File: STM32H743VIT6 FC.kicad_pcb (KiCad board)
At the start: 2 copper layers, 37 x 37 mm, 6 parts, among them J4 Conn_01x04_Male

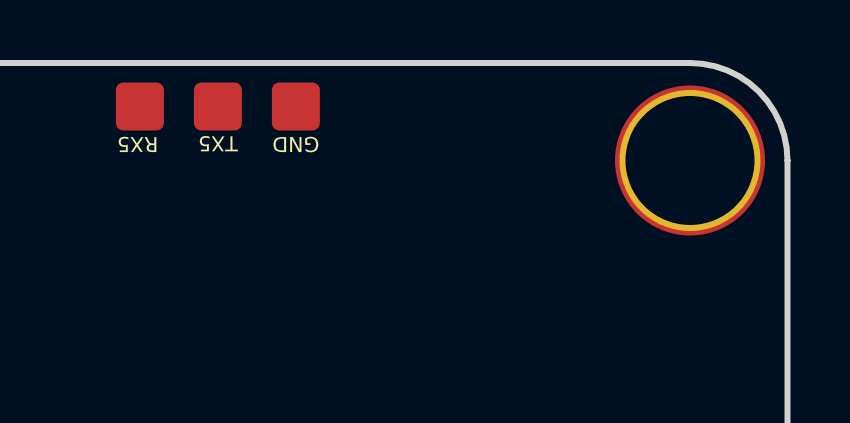
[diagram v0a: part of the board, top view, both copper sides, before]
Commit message: Added footprints.
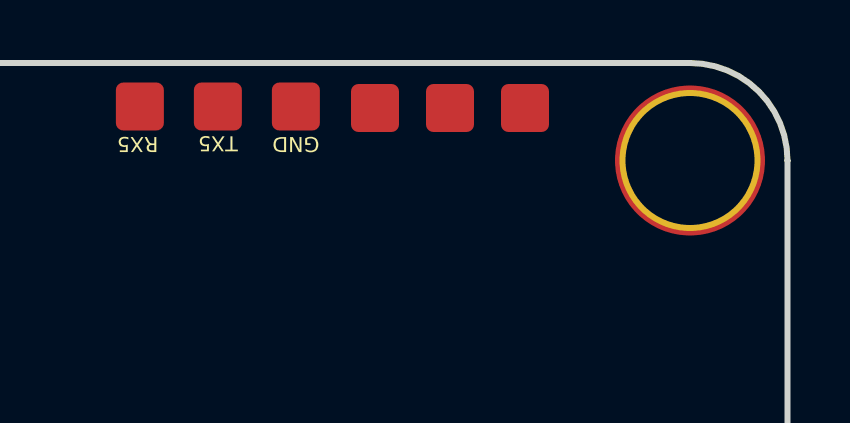
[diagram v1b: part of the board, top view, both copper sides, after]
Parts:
- added REF**: Pads_1x3, All:Pads_1x3, F.Cu at (173.0, 103.2)
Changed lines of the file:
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@@
+		(embedded_fonts no)
+	)
+	(footprint "All:Pads_1x3"
+		(layer "F.Cu")
+		(at 173 103.25)
+		(property "Reference" "REF**"
+			(at -0.3 1.1 0)
+			(unlocked yes)
+			(layer "F.SilkS")
+			(hide yes)
+			(effects
+				(font
+					(size 1 1)
+					(thickness 0.1)
+				)
+			)
+		)
+		(property "Value" "Pads_1x3"
+			(at 0 1 0)
+			(unlocked yes)
+			(layer "F.Fab")
+			(hide yes)
+			(effects
+				(font
+					(size 1 1)
+					(thickness 0.15)
+				)
+			)
+		)
+		(property "Datasheet" ""
+			(at 0 0 0)
+			(unlocked yes)
+			(layer "F.Fab")
+			(hide yes)
+			(effects
+				(font
+					(size 1 1)
+					(thickness 0.15)
+				)
+			)
+		)
+		(property "Description" ""
+			(at 0 0 0)
+			(unlocked yes)
+			(layer "F.Fab")
+			(hide yes)
+			(effects
+				(font
+					(size 1 1)
+					(thickness 0.15)
+				)
+			)
+		)
+		(attr smd)
+		(fp_line
+			(start -1.25 -1.25)
+			(end -1.25 1.25)
+			(stroke
+				(width 0.05)
+				(type solid)
+			)
+			(layer "F.CrtYd")
+		)
+		(fp_line
+			(start 1.25 -1.25)
+			(end 1.25 1.25)
+			(stroke
+				(width 0.05)
+				(type solid)
+			)
+			(layer "F.CrtYd")
+		)
+		(fp_rect
+			(start -3.75 -1.25)
+			(end 3.75 1.25)
+			(stroke
+				(width 0.05)
+				(type solid)
+			)
+			(fill no)
+			(layer "F.CrtYd")
+		)
+		(pad "1" smd roundrect
+			(at -2.5 0 180)
+			(size 1.6 1.6)
+			(layers "F.Cu" "F.Mask" "F.Paste")
+			(roundrect_rratio 0.15625)
+		)
+		(pad "2" smd roundrect
+			(at 0 0 180)
+			(size 1.6 1.6)
+			(layers "F.Cu" "F.Mask" "F.Paste")
+			(roundrect_rratio 0.15625)
+		)
+		(pad "3" smd roundrect
+			(at 2.5 0 180)
+			(size 1.6 1.6)
+			(layers "F.Cu" "F.Mask" "F.Paste")
+			(roundrect_rratio 0.15625)
+		)
 		(embedded_fonts no)
 	)

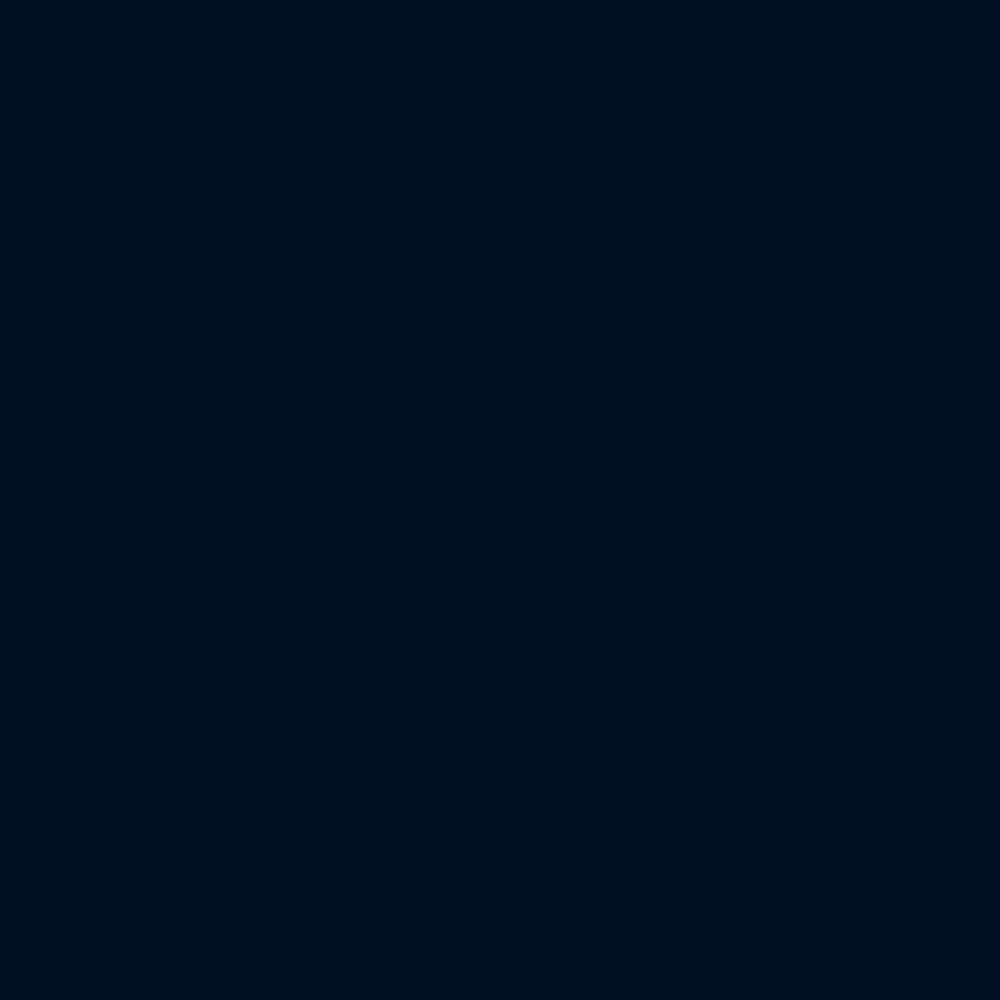
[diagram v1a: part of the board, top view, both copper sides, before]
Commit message: Added 3D models.
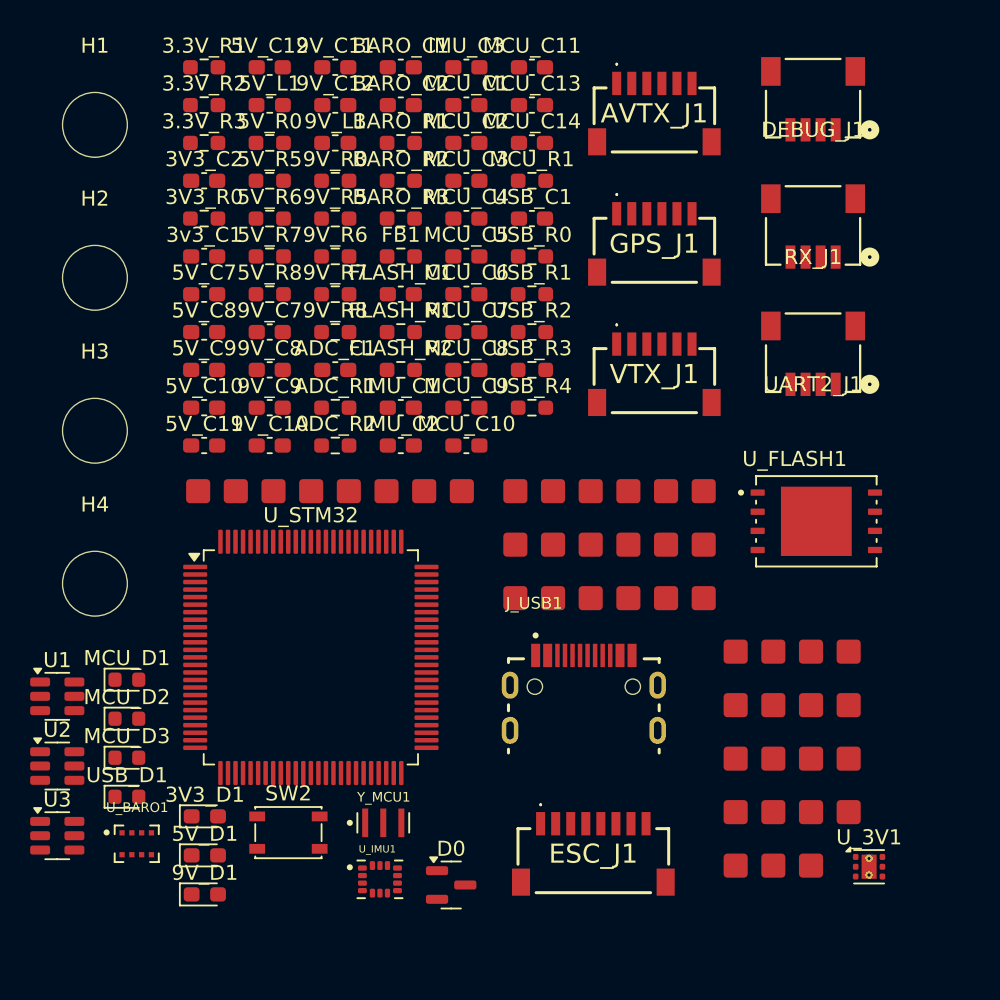
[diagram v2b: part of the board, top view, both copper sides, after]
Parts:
- added 3.3V_R1: 150, Resistor_SMD:R_0603_1608Metric_Pad0.98x0.95mm_HandSolder, F.Cu at (84.2, 36.8)
- added 3.3V_R2: 150, Resistor_SMD:R_0603_1608Metric_Pad0.98x0.95mm_HandSolder, F.Cu at (84.2, 39.3)
- added 3.3V_R3: 150, Resistor_SMD:R_0603_1608Metric_Pad0.98x0.95mm_HandSolder, F.Cu at (84.2, 41.8)
- added 3V3_C2: 1u, Capacitor_SMD:C_0603_1608Metric_Pad1.08x0.95mm_HandSolder, F.Cu at (84.2, 44.3)
- added 3V3_D1: RED, LED_SMD:LED_0603_1608Metric_Pad1.05x0.95mm_HandSolder, F.Cu at (84.3, 86.5)
- added 3V3_R0: 150, Resistor_SMD:R_0603_1608Metric_Pad0.98x0.95mm_HandSolder, F.Cu at (84.2, 46.8)
- added 3v3_C1: 1u, Capacitor_SMD:C_0603_1608Metric_Pad1.08x0.95mm_HandSolder, F.Cu at (84.2, 49.3)
- added 5V_C10: 22u, Capacitor_SMD:C_0603_1608Metric_Pad1.08x0.95mm_HandSolder, F.Cu at (84.2, 59.4)
- added 5V_C11: 22u, Capacitor_SMD:C_0603_1608Metric_Pad1.08x0.95mm_HandSolder, F.Cu at (84.2, 61.9)
- added 5V_C12: 75p, Capacitor_SMD:C_0603_1608Metric_Pad1.08x0.95mm_HandSolder, F.Cu at (88.6, 36.8)
- added 5V_C7: 10u, Capacitor_SMD:C_0603_1608Metric_Pad1.08x0.95mm_HandSolder, F.Cu at (84.2, 51.9)
- added 5V_C8: 100n, Capacitor_SMD:C_0603_1608Metric_Pad1.08x0.95mm_HandSolder, F.Cu at (84.2, 54.4)
- added 5V_C9: 100n, Capacitor_SMD:C_0603_1608Metric_Pad1.08x0.95mm_HandSolder, F.Cu at (84.2, 56.9)
- added 5V_D1: RED, LED_SMD:LED_0603_1608Metric_Pad1.05x0.95mm_HandSolder, F.Cu at (84.3, 89.1)
- added 5V_L1: 10u, Inductor_SMD:L_0603_1608Metric_Pad1.05x0.95mm_HandSolder, F.Cu at (88.6, 39.3)
- added 5V_R0: 330, Resistor_SMD:R_0603_1608Metric_Pad0.98x0.95mm_HandSolder, F.Cu at (88.6, 41.8)
- added 5V_R5: 511k, Resistor_SMD:R_0603_1608Metric_Pad0.98x0.95mm_HandSolder, F.Cu at (88.6, 44.3)
- added 5V_R6: 105k, Resistor_SMD:R_0603_1608Metric_Pad0.98x0.95mm_HandSolder, F.Cu at (88.6, 46.8)
- added 5V_R7: 100k, Resistor_SMD:R_0603_1608Metric_Pad0.98x0.95mm_HandSolder, F.Cu at (88.6, 49.3)
- added 5V_R8: 13k, Resistor_SMD:R_0603_1608Metric_Pad0.98x0.95mm_HandSolder, F.Cu at (88.6, 51.9)
- added 9V_C10: 22u, Capacitor_SMD:C_0603_1608Metric_Pad1.08x0.95mm_HandSolder, F.Cu at (88.6, 61.9)
- added 9V_C11: 22u, Capacitor_SMD:C_0603_1608Metric_Pad1.08x0.95mm_HandSolder, F.Cu at (92.9, 36.8)
- added 9V_C12: 75p, Capacitor_SMD:C_0603_1608Metric_Pad1.08x0.95mm_HandSolder, F.Cu at (92.9, 39.3)
- added 9V_C7: 10u, Capacitor_SMD:C_0603_1608Metric_Pad1.08x0.95mm_HandSolder, F.Cu at (88.6, 54.4)
- added 9V_C8: 100n, Capacitor_SMD:C_0603_1608Metric_Pad1.08x0.95mm_HandSolder, F.Cu at (88.6, 56.9)
- added 9V_C9: 100n, Capacitor_SMD:C_0603_1608Metric_Pad1.08x0.95mm_HandSolder, F.Cu at (88.6, 59.4)
- added 9V_D1: RED, LED_SMD:LED_0603_1608Metric_Pad1.05x0.95mm_HandSolder, F.Cu at (84.3, 91.7)
- added 9V_L1: 15u, Inductor_SMD:L_0603_1608Metric_Pad1.05x0.95mm_HandSolder, F.Cu at (92.9, 41.8)
- added 9V_R0: 750, Resistor_SMD:R_0603_1608Metric_Pad0.98x0.95mm_HandSolder, F.Cu at (92.9, 44.3)
- added 9V_R5: 511k, Resistor_SMD:R_0603_1608Metric_Pad0.98x0.95mm_HandSolder, F.Cu at (92.9, 46.8)
- added 9V_R6: 105k, Resistor_SMD:R_0603_1608Metric_Pad0.98x0.95mm_HandSolder, F.Cu at (92.9, 49.3)
- added 9V_R7: 100k, Resistor_SMD:R_0603_1608Metric_Pad0.98x0.95mm_HandSolder, F.Cu at (92.9, 51.9)
- added 9V_R8: 7k, Resistor_SMD:R_0603_1608Metric_Pad0.98x0.95mm_HandSolder, F.Cu at (92.9, 54.4)
- added ADC_C1: 100n, Capacitor_SMD:C_0603_1608Metric_Pad1.08x0.95mm_HandSolder, F.Cu at (92.9, 56.9)
- added ADC_R1: 15k, Resistor_SMD:R_0603_1608Metric_Pad0.98x0.95mm_HandSolder, F.Cu at (92.9, 59.4)
- added ADC_R2: 15k, Resistor_SMD:R_0603_1608Metric_Pad0.98x0.95mm_HandSolder, F.Cu at (92.9, 61.9)
- added AVTX_J1: SM06B-SRSS-TB, All:SM06BSRSSTBLFSN, F.Cu at (114.1, 40.1)
- added AVTX_J2: pads, All:Pads_1x6, F.Cu at (111.1, 64.9)
- added BARO_C1: 100n, Capacitor_SMD:C_0603_1608Metric_Pad1.08x0.95mm_HandSolder, F.Cu at (97.3, 36.8)
- added BARO_C2: 100n, Capacitor_SMD:C_0603_1608Metric_Pad1.08x0.95mm_HandSolder, F.Cu at (97.3, 39.3)
- added BARO_R1: 10k, Resistor_SMD:R_0603_1608Metric_Pad0.98x0.95mm_HandSolder, F.Cu at (97.3, 41.8)
- added BARO_R2: 10k, Resistor_SMD:R_0603_1608Metric_Pad0.98x0.95mm_HandSolder, F.Cu at (97.3, 44.3)
- added BARO_R3: 10k, Resistor_SMD:R_0603_1608Metric_Pad0.98x0.95mm_HandSolder, F.Cu at (97.3, 46.8)
- added CAM_J2: pads, All:Pads_1x3, F.Cu at (122.0, 89.8)
- added D0: BAT54C, Package_TO_SOT_SMD:SOT-23, F.Cu at (100.6, 91.1)
- added DEBUG_J1: SM04B-SRSS-TB, All:CONN_SM04B-SRSS-TB_JST, F.Cu at (124.6, 38.8)
- added DEBUG_J2: pads, All:Pads_1x4, F.Cu at (123.3, 75.6)
- added ESC_J1: SM08B-SRSS-TB, All:SM08BSRSSTB, F.Cu at (110.1, 89.3)
- added ESC_J2: pads, All:Pads_1x8, F.Cu at (92.6, 64.9)
- added FB1: FCM 1608KF-102T02, Resistor_SMD:R_0603_1608Metric_Pad0.98x0.95mm_HandSolder, F.Cu at (97.3, 49.3)
- added FLASH_C1: 100n, Capacitor_SMD:C_0603_1608Metric_Pad1.08x0.95mm_HandSolder, F.Cu at (97.3, 51.9)
- added FLASH_R1: 10k, Resistor_SMD:R_0603_1608Metric_Pad0.98x0.95mm_HandSolder, F.Cu at (97.3, 54.4)
- added FLASH_R2: 10k, Resistor_SMD:R_0603_1608Metric_Pad0.98x0.95mm_HandSolder, F.Cu at (97.3, 56.9)
- added GPS_J1: SM06B-SRSS-TB, All:SM06BSRSSTBLFSN, F.Cu at (114.1, 48.8)
- added GPS_J2: pads, All:Pads_1x6, F.Cu at (111.1, 68.5)
- added H1: MountingHole, MountingHole:MountingHole_4.3mm_M4, F.Cu at (77.0, 40.6)
- added H2: MountingHole, MountingHole:MountingHole_4.3mm_M4, F.Cu at (77.0, 50.8)
- added H3: MountingHole, MountingHole:MountingHole_4.3mm_M4, F.Cu at (77.0, 60.9)
- added H4: MountingHole, MountingHole:MountingHole_4.3mm_M4, F.Cu at (77.0, 71.1)
- added IMU_C1: 100n, Capacitor_SMD:C_0603_1608Metric_Pad1.08x0.95mm_HandSolder, F.Cu at (97.3, 59.4)
- added IMU_C2: 2u2, Capacitor_SMD:C_0603_1608Metric_Pad1.08x0.95mm_HandSolder, F.Cu at (97.3, 61.9)
- added IMU_C3: 10n, Capacitor_SMD:C_0603_1608Metric_Pad1.08x0.95mm_HandSolder, F.Cu at (101.6, 36.8)
- added J_USB1: USB4730-GF-A, All:GCT_USB4730-GF-A_REVA, F.Cu at (109.4, 80.8)
- added MCU_C1: 4u7, Capacitor_SMD:C_0603_1608Metric_Pad1.08x0.95mm_HandSolder, F.Cu at (101.6, 39.3)
- added MCU_C10: 1u, Capacitor_SMD:C_0603_1608Metric_Pad1.08x0.95mm_HandSolder, F.Cu at (101.6, 61.9)
- added MCU_C11: 100n, Capacitor_SMD:C_0603_1608Metric_Pad1.08x0.95mm_HandSolder, F.Cu at (106.0, 36.8)
- added MCU_C13: 2u2, Capacitor_SMD:C_0603_1608Metric_Pad1.08x0.95mm_HandSolder, F.Cu at (106.0, 39.3)
- added MCU_C14: 2u2, Capacitor_SMD:C_0603_1608Metric_Pad1.08x0.95mm_HandSolder, F.Cu at (106.0, 41.8)
- added MCU_C2: 100n, Capacitor_SMD:C_0603_1608Metric_Pad1.08x0.95mm_HandSolder, F.Cu at (101.6, 41.8)
- added MCU_C3: 100n, Capacitor_SMD:C_0603_1608Metric_Pad1.08x0.95mm_HandSolder, F.Cu at (101.6, 44.3)
- added MCU_C4: 100n, Capacitor_SMD:C_0603_1608Metric_Pad1.08x0.95mm_HandSolder, F.Cu at (101.6, 46.8)
- added MCU_C5: 100n, Capacitor_SMD:C_0603_1608Metric_Pad1.08x0.95mm_HandSolder, F.Cu at (101.6, 49.3)
- added MCU_C6: 100n, Capacitor_SMD:C_0603_1608Metric_Pad1.08x0.95mm_HandSolder, F.Cu at (101.6, 51.9)
- added MCU_C7: 100n, Capacitor_SMD:C_0603_1608Metric_Pad1.08x0.95mm_HandSolder, F.Cu at (101.6, 54.4)
- added MCU_C8: 1u, Capacitor_SMD:C_0603_1608Metric_Pad1.08x0.95mm_HandSolder, F.Cu at (101.6, 56.9)
- added MCU_C9: 100n, Capacitor_SMD:C_0603_1608Metric_Pad1.08x0.95mm_HandSolder, F.Cu at (101.6, 59.4)
- added MCU_D1: RED, LED_SMD:LED_0603_1608Metric, F.Cu at (79.1, 77.4)
- added MCU_D2: RED, LED_SMD:LED_0603_1608Metric, F.Cu at (79.1, 80.0)
- added MCU_D3: RED, LED_SMD:LED_0603_1608Metric, F.Cu at (79.1, 82.6)
- added MCU_R1: 10K, Resistor_SMD:R_0603_1608Metric_Pad0.98x0.95mm_HandSolder, F.Cu at (106.0, 44.3)
- added OTHER_J2: pads, All:Pads_1x4, F.Cu at (123.3, 79.1)
- added RX_J1: SM04B-SRSS-TB, All:CONN_SM04B-SRSS-TB_JST, F.Cu at (124.6, 47.3)
- added RX_J2: pads, All:Pads_1x4, F.Cu at (123.3, 82.7)
- added SW2: Y78B22310FP, Button_Switch_SMD:SW_SPST_PTS810, F.Cu at (89.8, 87.6)
- added U1: TPS54302DDCR, Package_TO_SOT_SMD:SOT-23-6, F.Cu at (74.5, 78.5)
- added U2: USBLC6-2SC6, Package_TO_SOT_SMD:SOT-23-6, F.Cu at (74.5, 83.2)
- added U3: TPS54302DDCR, Package_TO_SOT_SMD:SOT-23-6, F.Cu at (74.5, 87.8)
- added UART2_J1: SM04B-SRSS-TB, All:CONN_SM04B-SRSS-TB_JST, F.Cu at (124.6, 55.7)
- added UART2_J2: pads, All:Pads_1x4, F.Cu at (123.3, 86.2)
- added USB_C1: 100n, Capacitor_SMD:C_0603_1608Metric_Pad1.08x0.95mm_HandSolder, F.Cu at (106.0, 46.8)
- added USB_D1: RED, LED_SMD:LED_0603_1608Metric, F.Cu at (79.1, 85.2)
- added USB_R0: 330, Resistor_SMD:R_0603_1608Metric_Pad0.98x0.95mm_HandSolder, F.Cu at (106.0, 49.3)
- added USB_R1: 5k1, Resistor_SMD:R_0603_1608Metric_Pad0.98x0.95mm_HandSolder, F.Cu at (106.0, 51.9)
- added USB_R2: 5k1, Resistor_SMD:R_0603_1608Metric_Pad0.98x0.95mm_HandSolder, F.Cu at (106.0, 54.4)
- added USB_R3: 22, Resistor_SMD:R_0603_1608Metric_Pad0.98x0.95mm_HandSolder, F.Cu at (106.0, 56.9)
- added USB_R4: 22, Resistor_SMD:R_0603_1608Metric_Pad0.98x0.95mm_HandSolder, F.Cu at (106.0, 59.4)
- added U_3V1: LP5912-3.3DRV, Package_SON:WSON-6-1EP_2x2mm_P0.65mm_EP1x1.6mm_ThermalVias, F.Cu at (128.4, 89.8)
- added U_BARO1: DPS310, All:XDCR_DPS310, F.Cu at (79.8, 88.3)
- added U_FLASH1: W25N01GVZEIT, All:SON127P600X800X80-9N, F.Cu at (124.9, 66.9)
- added U_IMU1: ICM-42688-P, All:PQFN50P300X250X97-14N, F.Cu at (95.9, 90.7)
- added U_STM32: STM32H743VIT6, Package_QFP:LQFP-100_14x14mm_P0.5mm, F.Cu at (91.3, 76.0)
- added VTX_J1: SM06B-SRSS-TB, All:SM06BSRSSTBLFSN, F.Cu at (114.1, 57.4)
- added VTX_J2: pads, All:Pads_1x6, F.Cu at (111.1, 72.0)
- added Y_MCU1: CSTNE8M00G520000R0, All:OSC_CSTNE8M00G520000R0, F.Cu at (96.1, 86.9)

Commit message: pushhhh
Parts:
- removed the H1 at (77.0, 40.6)
- removed the H2 at (77.0, 50.8)
- removed the H3 at (77.0, 60.9)
- removed the H4 at (77.0, 71.1)
- removed J4: Conn_01x04_Male, Connector_Pin:solderpads1x04
- removed REF**: Pads_1x3, All:Pads_1x3
- moved ESC_J1 46.2 mm to (148.0, 63.0)
- moved 3.3V_R2 29.8 mm to (75.5, 67.8)
- moved 5V_C10 29.8 mm to (75.5, 87.9)
- moved 5V_C7 29.8 mm to (75.5, 80.4)
- moved 5V_L1 29.8 mm to (79.8, 67.8)
- moved 5V_R8 29.8 mm to (79.8, 80.4)
- moved 9V_C12 29.8 mm to (84.2, 67.8)
- moved 9V_C9 29.8 mm to (79.8, 87.9)
- moved 9V_R7 29.8 mm to (84.2, 80.4)
- moved ADC_R1 29.8 mm to (84.2, 87.9)
- moved BARO_C2 29.8 mm to (88.5, 67.8)
- moved FLASH_C1 29.8 mm to (88.5, 80.4)
- moved IMU_C1 29.8 mm to (88.5, 87.9)
- moved MCU_C1 29.8 mm to (92.9, 67.8)
- moved MCU_C13 29.8 mm to (97.2, 67.8)
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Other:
- board text removed: "GND"
- board text removed: "RX5"
- board text removed: "TX5"

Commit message: Fixed usb footprint.
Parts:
- removed J_USB1: USB4730-GF-A, All:GCT_USB4730-GF-A_REVA
- added H1: MountingHole, MountingHole:MountingHole_4.3mm_M4, F.Cu at (4.58, 4.58)
- added H2: MountingHole, MountingHole:MountingHole_4.3mm_M4, F.Cu at (4.58, 14.7)
- added H3: MountingHole, MountingHole:MountingHole_4.3mm_M4, F.Cu at (4.58, 24.9)
- added H4: MountingHole, MountingHole:MountingHole_4.3mm_M4, F.Cu at (4.58, 35.0)
- added J1: USB4730-GF-A_REVA, All:GCT_USB4730-GF-A_REVA, F.Cu at (101.9, 128.5)
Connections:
- U2 pad 1: Net-(J_USB1-D+-PadA6) -> /DP
- U2 pad 3: Net-(J_USB1-D--PadA7) -> /DN
- USB_R1 pad 1: Net-(J_USB1-CC1) -> GND
- USB_R1 pad 2: GND -> Net-(J1-CC1)
- USB_R2 pad 1: GND -> Net-(J1-CC2)
- USB_R2 pad 2: Net-(J_USB1-CC2) -> GND

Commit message: minor
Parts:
- removed the H1 at (4.58, 4.58)
- removed the H2 at (4.58, 14.7)
- removed the H3 at (4.58, 24.9)
- removed the H4 at (4.58, 35.0)
- AVTX_J1, DEBUG_J1, DEBUG_J2, ESC_J1, GPS_J1, RX_J1, UART2_J1, VTX_J1: moved to B.Cu
- moved DEBUG_J1 113.0 mm to (95.1, 167.7)
- moved AVTX_J1 110.6 mm to (84.6, 166.4)
- moved RX_J1 97.3 mm to (95.1, 159.2)
- moved GPS_J1 94.5 mm to (84.6, 157.7)
- moved ESC_J1 86.8 mm to (126.3, 147.1)
- moved UART2_J1 82.0 mm to (95.1, 150.8)
- moved VTX_J1 79.0 mm to (84.6, 149.1)
- moved MCU_D1 59.8 mm to (128.0, 89.9)
- moved MCU_D2 59.8 mm to (128.0, 92.5)
- moved U1 59.8 mm to (123.3, 91.0)
- moved U2 59.8 mm to (123.3, 95.6)
- moved U3 59.8 mm to (123.3, 100.2)
- moved MCU_D3 59.8 mm to (128.0, 95.0)
- moved USB_D1 59.8 mm to (128.0, 97.6)
- moved 3V3_D1 54.6 mm to (128.1, 100.2)
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
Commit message: boom
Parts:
- removed AVTX_J1: SM06B-SRSS-TB, All:SM06BSRSSTBLFSN
- removed BARO_C1, BARO_C2: 100n, Capacitor_SMD:C_0603_1608Metric_Pad1.08x0.95mm_HandSolder
- removed BARO_R1, BARO_R2, BARO_R3: 10k, Resistor_SMD:R_0603_1608Metric_Pad0.98x0.95mm_HandSolder
- removed DEBUG_J1, RX_J1, UART2_J1: SM04B-SRSS-TB, All:CONN_SM04B-SRSS-TB_JST
- removed U_BARO1: DPS310, All:XDCR_DPS310
- MCU_D1, MCU_D2, MCU_D3, USB_D1: footprint LED_SMD:LED_0603_1608Metric -> LED_SMD:LED_0603_1608Metric_Pad1.05x0.95mm_HandSolder
- moved J1 73.0 mm to (180.9, 115.2), turned to 90 degrees
- moved ESC_J2 72.1 mm to (164.0, 137.5)
- moved MCU_D1 61.5 mm to (176.1, 128.1)
- moved U_FLASH1 61.1 mm to (163.1, 106.1), turned to 180 degrees
- moved MCU_D2 61.1 mm to (176.1, 130.0)
- moved MCU_D3 60.7 mm to (176.1, 132.0)
- moved RX_J2 60.4 mm to (182.8, 126.5), turned to 90 degrees
- moved USB_D1 60.3 mm to (176.1, 133.9)
- moved VTX_J2 59.3 mm to (166.5, 134.9)
- moved UART2_J2 56.6 mm to (172.8, 104.2)
- moved U3 55.6 mm to (170.0, 130.5)
- moved U1 54.7 mm to (160.9, 130.7), turned to -90 degrees
- moved U_STM32 54.1 mm to (161.2, 119.0)
- moved OTHER_J2 52.9 mm to (172.8, 106.8)
- moved 3V3_D1 52.9 mm to (176.1, 122.4)
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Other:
- copper layers 2 -> 4

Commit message: posoki
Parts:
- 5V_C10, 5V_C11, 5V_C12, 5V_C7, 5V_C8, 5V_C9, 5V_L1, 5V_R0, 5V_R5, 5V_R6, 5V_R7, 5V_R8, 9V_C10, 9V_C11, 9V_C12, 9V_C7, 9V_C8, 9V_C9, 9V_L1, 9V_R0, 9V_R5, 9V_R6, 9V_R7, 9V_R8, ADC_C1, ADC_R1, ADC_R2, FLASH_C1, FLASH_R1, FLASH_R2, U1, U3, U_FLASH1: moved to B.Cu
- moved U1 30.8 mm to (136.0, 148.9), turned to 90 degrees
- moved U3 30.8 mm to (145.1, 148.7)
- moved U_FLASH1 17.3 mm to (153.4, 91.8)

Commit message: mmm
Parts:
- moved ESC_J2 5.71 mm to (164.1, 143.2)
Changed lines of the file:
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@@
 		)
 		(fp_line
+			(start 0 -1.25)
+			(end 0 1.25)
+			(stroke
+				(width 0.05)
+				(type solid)
+			)
+			(layer "F.CrtYd")
+		)
+		(fp_line
 			(start -2.5 -1.25)
 			(end -2.5 1.25)
@@
 		)
 		(fp_line
+			(start 0 -1.25)
+			(end 0 1.25)
+			(stroke
+				(width 0.05)
+				(type solid)
+			)
+			(layer "F.CrtYd")
+		)
+		(fp_line
 			(start 2.5 -1.25)
 			(end 2.5 1.25)
@@
 	(footprint "All:Pads_1x8"
 		(layer "F.Cu")
-		(at 164 137.5)
+		(at 164.1332 143.2052)
 		(property "Reference" "ESC_J2"
 			(at -0.3 1.1 0)
@@
 		)
 		(fp_line
+			(start -5 -1.25)
+			(end -5 1.25)
+			(stroke
+				(width 0.05)
+				(type solid)
+			)
+			(layer "F.CrtYd")
+		)
+		(fp_line
 			(start -2.5 -1.25)
 			(end -2.5 1.25)
@@
 		)
 		(fp_line
+			(start 5 -1.25)
+			(end 5 1.25)
+			(stroke
+				(width 0.05)
+				(type solid)
+			)
+			(layer "F.CrtYd")
+		)
+		(fp_line
 			(start 7.5 -1.25)
 			(end 7.5 1.25)
@@
 			(stroke
 				(width 0.05)
+				(type solid)
+			)
+			(layer "F.CrtYd")
+		)
+		(fp_line
+			(start 0 -1.25)
+			(end 0 1.25)
+			(stroke
+				(width 0.05)
